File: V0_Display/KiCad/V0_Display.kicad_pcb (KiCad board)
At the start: 2 copper layers, 80 x 35 mm, 31 parts, among them J1 USB_B_Micro, J2 I2C Header 1, J3 Conn_01x03, J4 Conn_01x02, J5 SWD Header, J6 I2C Header 2, J7 USB_Header, J8 Conn_01x02, SW1 SW_SPST, SW2 SW_SPST, SW3 SW_SPST, SW4 SW_SPST, SW5 SW_SPST, SW6 SW_SPST, SW7 Rotary_Encoder_Switch, U1 AP2127K-3.3, U2 STM32F042F6Px, U3 74LVC1G17

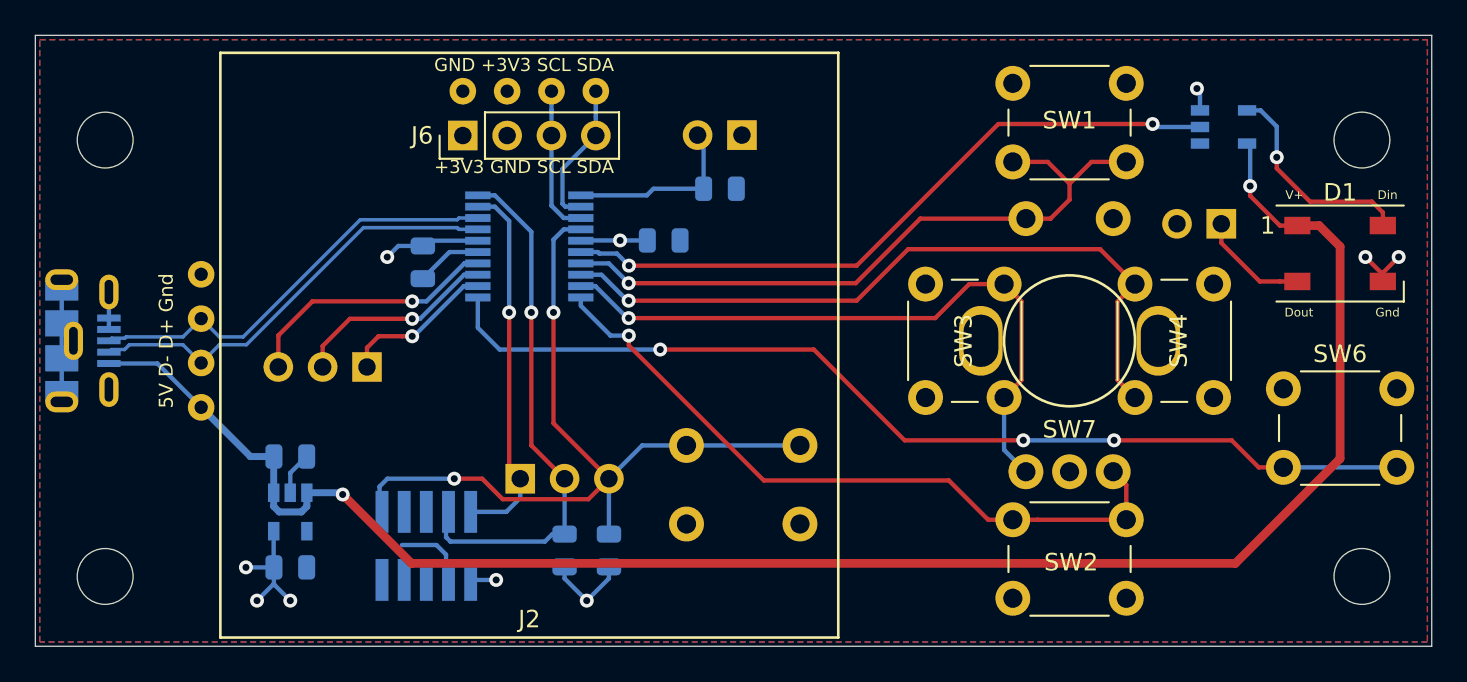
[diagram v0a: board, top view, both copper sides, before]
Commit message: Library update, change to universal pin-out (#37)
* Libray update, change to universal pinout

* Update README.md

Update readme to remove 0.9" OLED support
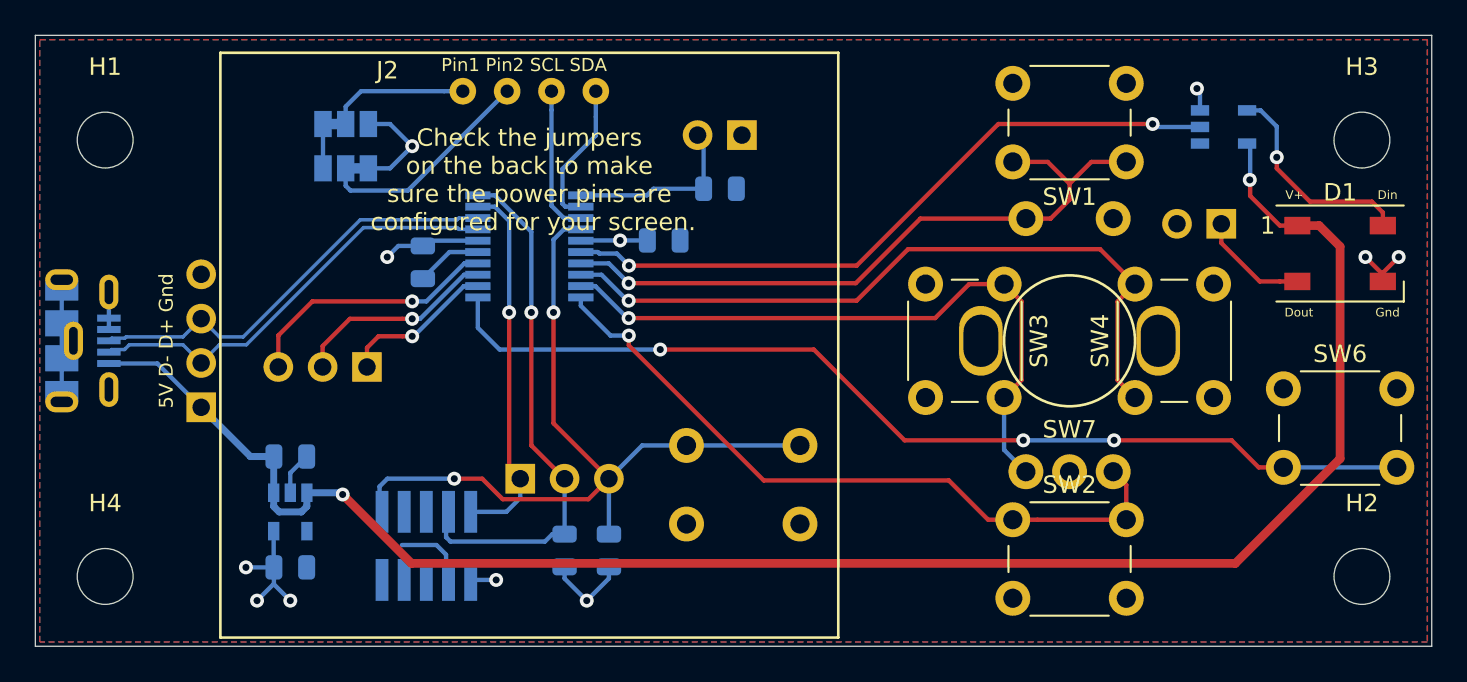
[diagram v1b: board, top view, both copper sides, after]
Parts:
- removed J6: I2C Header 2, Connector_PinHeader_2.54mm:PinHeader_1x04_P2.54mm_Vertical
- added G***: LOGO, V0-Display:VoronLogo_6pt5mm_silkScreen, B.Cu at (144.4, 67.2)
- added JP1: Pin2, V0-Display:SolderJumper-3_P1.3mm_Bridged12_Pad1.0x1.5mm, B.Cu at (103.0, 57.3)
- added JP2: Pin1, V0-Display:SolderJumper-3_P1.3mm_Bridged12_Pad1.0x1.5mm, B.Cu at (103.0, 54.7)
- C1, C2, C3, C4: footprint Capacitor_SMD:C_0805_2012Metric -> V0-Display:C_0805_2012Metric
- D1: footprint LED_SMD:LED_WS2812B_PLCC4_5.0x5.0mm_P3.2mm -> V0-Display:LED_WS2812B_PLCC4_5.0x5.0mm_P3.2mm
- GPIO1: footprint Connector_PinHeader_2.54mm:PinHeader_1x03_P2.54mm_Horizontal -> V0-Display:PinHeader_1x03_P2.54mm_Vertical
- H1, H2, H3, H4: footprint MountingHole:MountingHole_3.2mm_M3 -> V0-Display:MountingHole_3.2mm_M3
- J1: footprint TRA_KiCad_Footprints:MolexVertical&Horizontal_MicroB -> V0-Display:MolexVertical&Horizontal_MicroB
- J2: footprint TRA_KiCad_Footprints:1pt3in_OLED -> V0-Display:1pt3in_OLED
- J3: footprint Connector_PinHeader_2.54mm:PinHeader_1x03_P2.54mm_Vertical -> V0-Display:PinHeader_1x03_P2.54mm_Vertical
- J4, J8: footprint Connector_PinHeader_2.54mm:PinHeader_1x02_P2.54mm_Vertical -> V0-Display:PinHeader_1x02_P2.54mm_Vertical
- J5: footprint Connector_PinHeader_1.27mm:PinHeader_2x05_P1.27mm_Vertical_SMD -> V0-Display:PinHeader_2x05_P1.27mm_Vertical_SMD
- J7: footprint TRA_KiCad_Footprints:01x04_unpopulated -> V0-Display:PinHeader_1x04_P2.54mm_Vertical
- R1, R2, R3: footprint Resistor_SMD:R_0805_2012Metric -> V0-Display:R_0805_2012Metric
- SW1, SW2, SW3, SW4: footprint Button_Switch_THT:SW_PUSH_6mm_H9.5mm -> V0-Display:SW_PUSH_6mm
- SW5, SW6: footprint Button_Switch_THT:SW_PUSH_6mm -> V0-Display:SW_PUSH_6mm
- SW7: footprint TRA_KiCad_Footprints:EN11_Encoder -> V0-Display:EN11_Encoder
- U1: footprint Package_TO_SOT_SMD:SOT-23-5 -> V0-Display:SOT-23-5
- U2: footprint Package_SO:TSSOP-20_4.4x6.5mm_P0.65mm -> V0-Display:TSSOP-20_4.4x6.5mm_P0.65mm
- U3: footprint digikey-footprints:SOT-753 -> V0-Display:SOT-753
- moved J7 3.81 mm to (94.7, 71.0), turned to 0 degrees
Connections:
- J2 pad 1: GND -> Pin1
- J2 pad 2: +3V3 -> Pin2
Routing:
- net Pin2: track 0.00 -> 12.7 mm
- net Pin1: track 0.00 -> 8.07 mm
- net +3V3: track 23.2 -> 29.3 mm, vias 7 -> 8
- net GND: track 26.2 -> 28.7 mm
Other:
- board text added: "1 2 3 GPIO"
- board text added: "1(GND)"
- board text added: "1(VCC)"
- board text added: "2(GND)"
- board text added: "2(VCC)"
- board text added: "Check the jumpers on the back to make sure the power pins are configured for your screen."
- board text added: "Neo-Out Gnd"
- board text added: "Pin1 Pin2 SCL SDA"
- board text added: "SDA SCL Pin2 Pin1"
- board text added: "T. Abraham V0-Display Rev-C"
- board text removed: "+3V3 GND SCL SDA"
- board text removed: "GND +3V3 SCL SDA"
- board text removed: "GPIO 1 2 3"
- board text removed: "SDA SCL +3V3 GND"
- board text removed: "SDA SCL GND +3V3"
